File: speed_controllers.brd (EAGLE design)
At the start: 147.3 x 147.3 mm, 46 parts, among them M1 TE-1-1123723-3, M2 TE-1-1123723-3, M3 TE-1-1123723-3, M4 TE-1-1123723-3, M5 TE-1-1123723-3, M6 TE-1-1123723-3, M7 TE-1-1123723-3, M8 TE-1-1123723-3

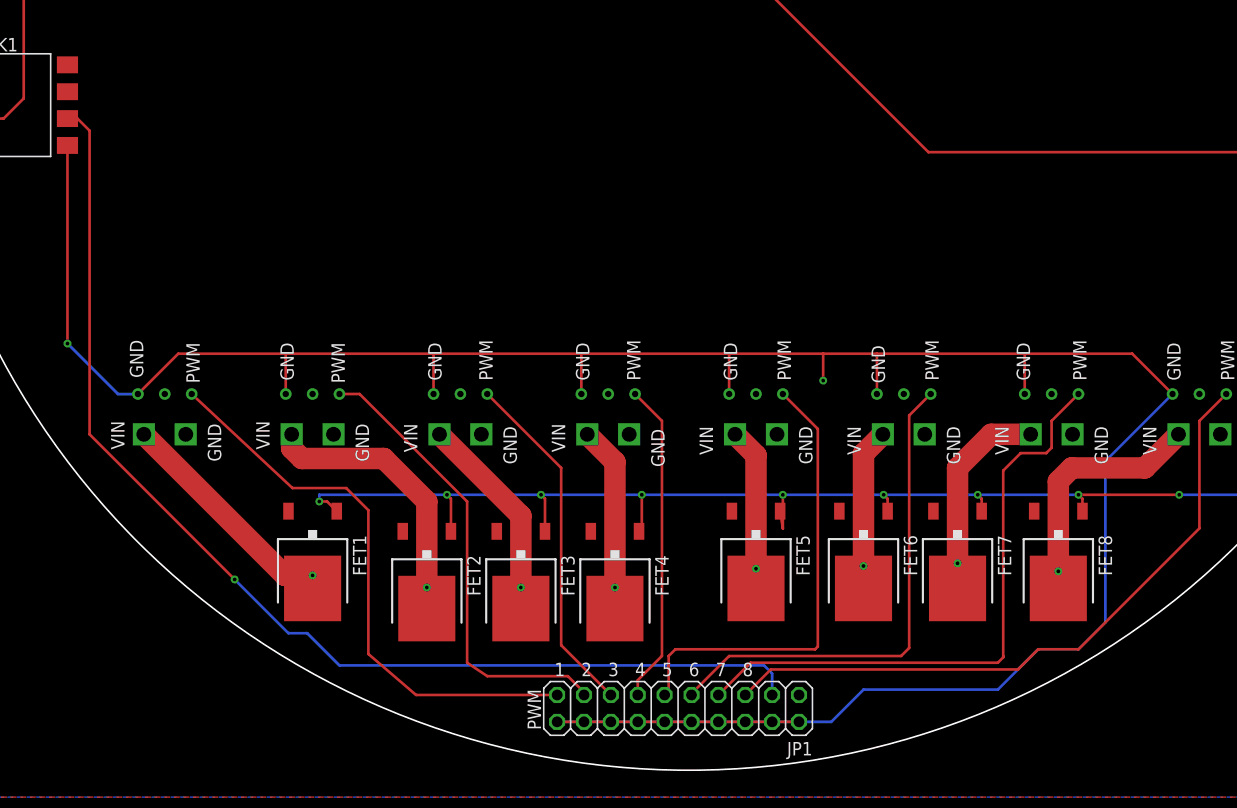
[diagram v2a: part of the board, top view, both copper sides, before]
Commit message: Changed Optocoupler circuit
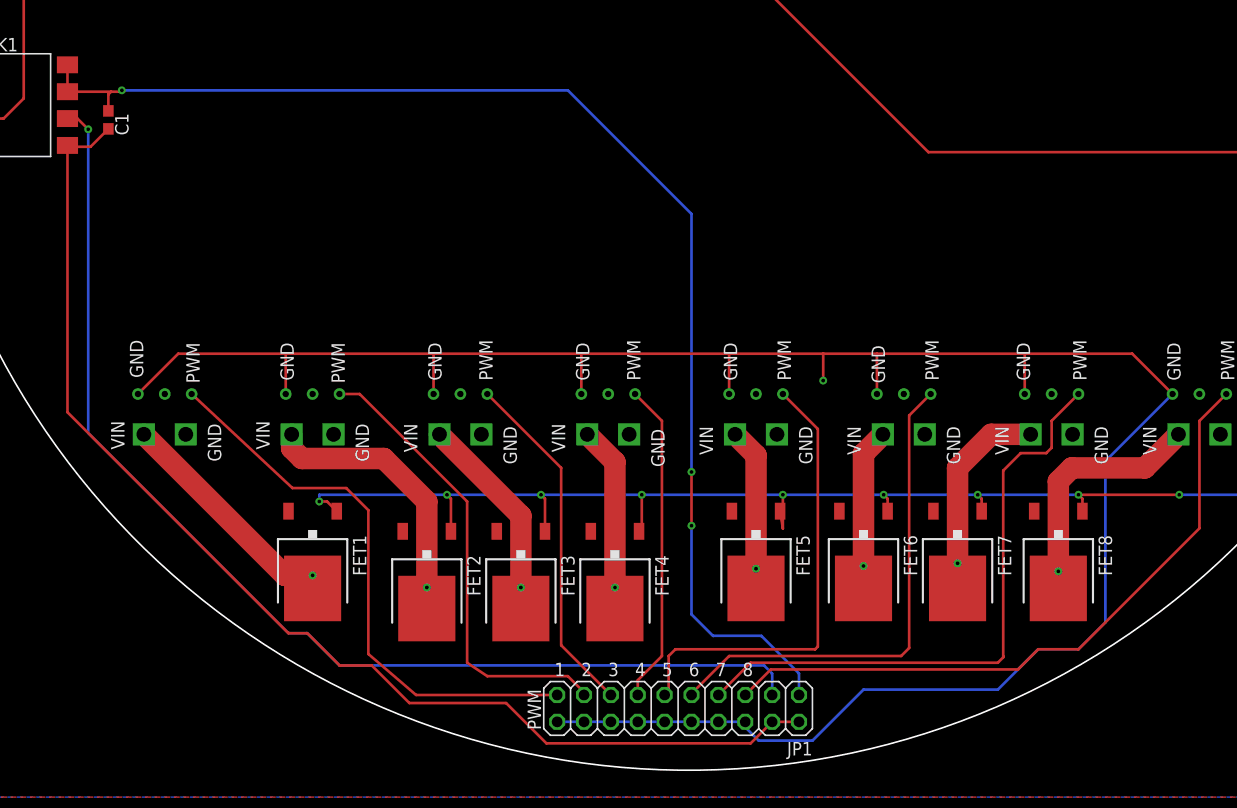
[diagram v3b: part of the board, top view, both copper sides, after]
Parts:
- added C1: 100nF, rcl:C0603
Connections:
- new net MCU_GND: C1.2, JP1.2, JP1.4, OK1.5
- new net MCU_VCC: C1.1, JP1.1, OK1.7, OK1.8
- net PWM_GND: no longer JP1.2, JP1.4, OK1.5
- net VCC: no longer OK1.7, OK1.8
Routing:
- net MCU_VCC: track 0.00 -> 120.7 mm, vias 0 -> 3
- net MCU_GND: track 0.00 -> 112.7 mm
- net PWM_GND: track 256.5 -> 208.0 mm, vias 2 -> 1

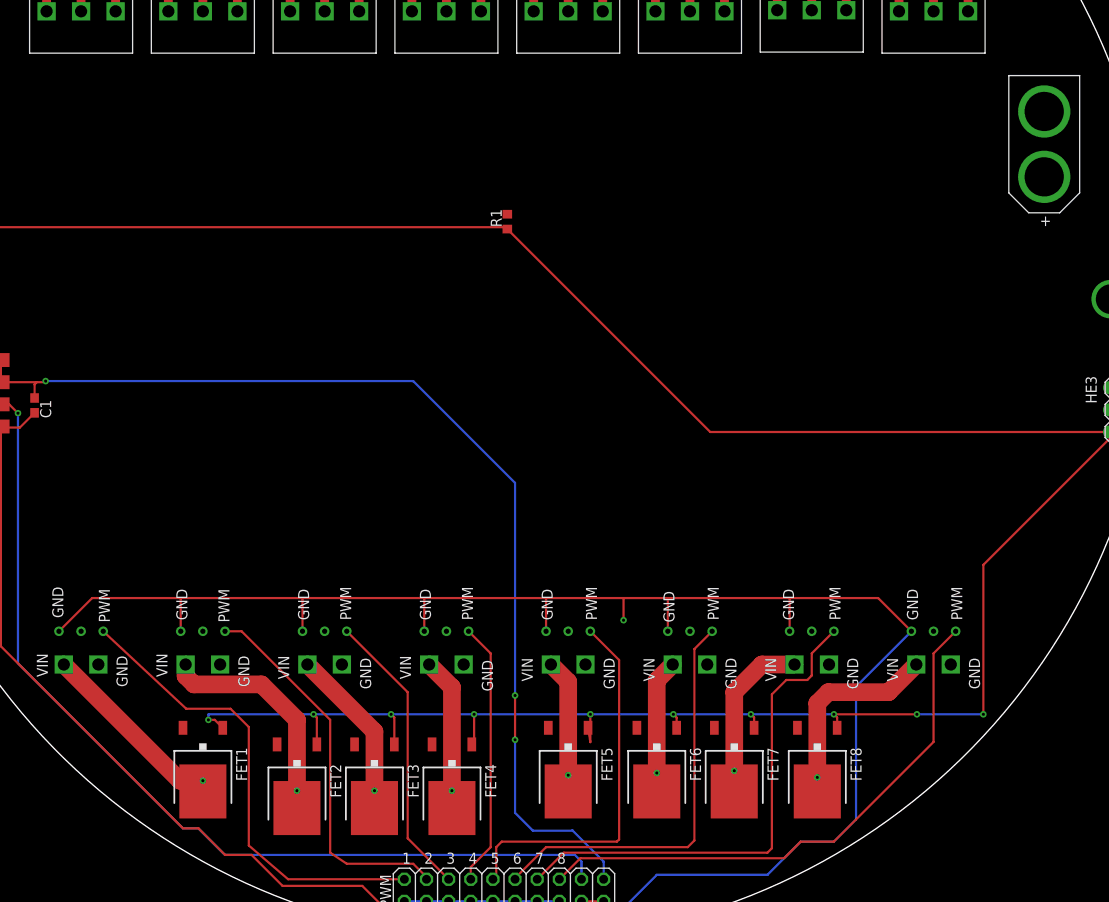
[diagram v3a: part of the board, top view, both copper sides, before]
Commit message: Redid PWM and moved silkscreen for the XT-60
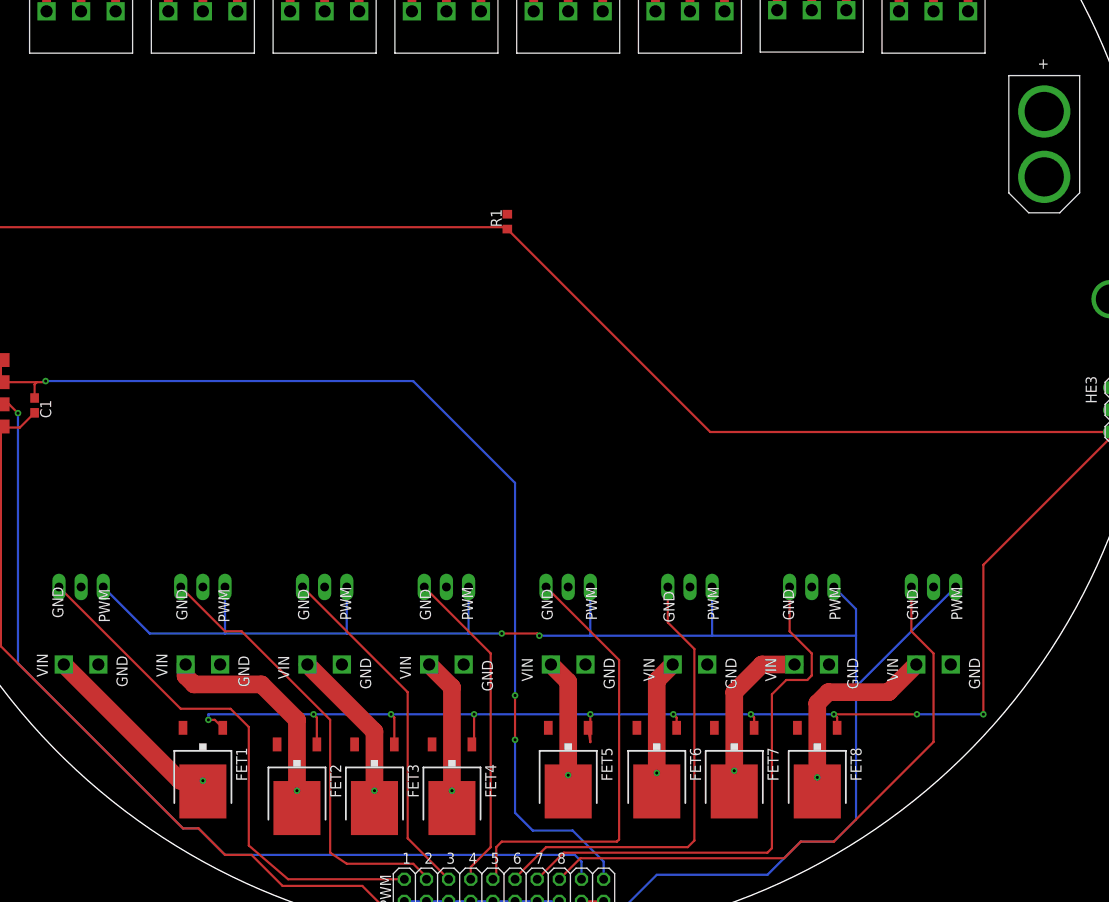
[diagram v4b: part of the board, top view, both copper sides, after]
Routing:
- net PWM_GND: track 208.0 -> 217.2 mm, vias 1 -> 2
- net SIG_1: track 53.9 -> 61.3 mm
- net SIG_4: track 30.8 -> 38.0 mm
- net SIG_5: track 43.5 -> 50.7 mm
- net SIG_3: track 33.3 -> 40.5 mm
- net SIG_2: track 43.8 -> 51.0 mm
- net SIG_6: track 47.3 -> 52.8 mm
- net SIG_8: track 63.2 -> 68.3 mm
- net SIG_7: track 57.6 -> 62.7 mm
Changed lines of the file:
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@@
 <text x="-44.196" y="-40.894" size="1.27" layer="26" rot="MR270">GND</text>
 <text x="-53.34" y="-40.64" size="1.27" layer="26" rot="MR270">VIN</text>
-<text x="60.452" y="8.382" size="1.27" layer="25">+</text>
+<text x="60.198" y="26.416" size="1.27" layer="25">+</text>
 </plain>
 <attributes>
@@
 <contactref element="MOTOR6" pad="PWM_GND"/>
 <contactref element="MOTOR5" pad="PWM_GND"/>
-<wire x1="45.72" y1="-38.1" x2="39.37" y2="-44.45" width="0.254" layer="16"/>
+<wire x1="50.8" y1="-33.02" x2="39.37" y2="-44.45" width="0.254" layer="16"/>
 <wire x1="39.37" y1="-44.45" x2="39.37" y2="-59.69" width="0.254" layer="16"/>
 <wire x1="39.37" y1="-59.69" x2="36.83" y2="-62.23" width="0.254" layer="16"/>
@@
 <contactref element="MOTOR3" pad="PWM_GND"/>
 <contactref element="MOTOR4" pad="PWM_GND"/>
-<wire x1="-52.07" y1="-38.1" x2="-48.26" y2="-34.29" width="0.254" layer="1"/>
-<wire x1="-48.26" y1="-34.29" x2="-38.1" y2="-34.29" width="0.254" layer="1"/>
-<wire x1="-38.1" y1="-34.29" x2="-24.13" y2="-34.29" width="0.254" layer="1"/>
-<wire x1="-24.13" y1="-34.29" x2="-10.16" y2="-34.29" width="0.254" layer="1"/>
-<wire x1="-10.16" y1="-34.29" x2="3.81" y2="-34.29" width="0.254" layer="1"/>
-<wire x1="3.81" y1="-34.29" x2="12.7" y2="-34.29" width="0.254" layer="1"/>
-<wire x1="12.7" y1="-34.29" x2="17.78" y2="-34.29" width="0.254" layer="1"/>
-<wire x1="17.78" y1="-34.29" x2="31.75" y2="-34.29" width="0.254" layer="1"/>
-<wire x1="41.91" y1="-34.29" x2="31.75" y2="-34.29" width="0.254" layer="1"/>
-<wire x1="-10.16" y1="-38.1" x2="-10.16" y2="-34.29" width="0.254" layer="1"/>
-<wire x1="-24.13" y1="-38.1" x2="-24.13" y2="-34.29" width="0.254" layer="1"/>
-<wire x1="-38.1" y1="-38.1" x2="-38.1" y2="-34.29" width="0.254" layer="1"/>
-<wire x1="12.7" y1="-34.29" x2="12.7" y2="-36.83" width="0.254" layer="1"/>
-<via x="12.7" y="-36.83" extent="1-16" drill="0.35"/>
 <contactref element="JP1" pad="20"/>
 <contactref element="JP1" pad="18"/>
@@
 <wire x1="5.334" y1="-69.596" x2="5.334" y2="-69.088" width="0.254" layer="16"/>
 <wire x1="16.51" y1="-66.04" x2="11.684" y2="-70.866" width="0.254" layer="16"/>
-<wire x1="3.81" y1="-38.1" x2="3.81" y2="-34.29" width="0.254" layer="1"/>
-<wire x1="17.78" y1="-38.1" x2="17.78" y2="-34.29" width="0.254" layer="1"/>
-<wire x1="31.75" y1="-38.1" x2="31.75" y2="-34.29" width="0.254" layer="1"/>
-<wire x1="45.72" y1="-38.1" x2="41.91" y2="-34.29" width="0.254" layer="1"/>
+<wire x1="39.37" y1="-44.45" x2="39.37" y2="-38.608" width="0.254" layer="16"/>
+<wire x1="39.37" y1="-38.608" x2="39.37" y2="-35.56" width="0.254" layer="16"/>
+<wire x1="39.37" y1="-35.56" x2="36.83" y2="-33.02" width="0.254" layer="16"/>
+<wire x1="39.37" y1="-38.608" x2="22.86" y2="-38.608" width="0.254" layer="16"/>
+<via x="3.048" y="-38.608" extent="1-16" drill="0.35"/>
+<wire x1="22.86" y1="-38.608" x2="8.89" y2="-38.608" width="0.254" layer="16"/>
+<wire x1="8.89" y1="-38.608" x2="3.048" y2="-38.608" width="0.254" layer="16"/>
+<wire x1="3.048" y1="-38.608" x2="2.794" y2="-38.354" width="0.254" layer="1"/>
+<wire x1="2.794" y1="-38.354" x2="-1.27" y2="-38.354" width="0.254" layer="1"/>
+<via x="-1.27" y="-38.354" extent="1-16" drill="0.35"/>
+<wire x1="-1.27" y1="-38.354" x2="-5.08" y2="-38.354" width="0.254" layer="16"/>
+<wire x1="-5.08" y1="-38.354" x2="-19.05" y2="-38.354" width="0.254" layer="16"/>
+<wire x1="-19.05" y1="-38.354" x2="-33.02" y2="-38.354" width="0.254" layer="16"/>
+<wire x1="-33.02" y1="-38.354" x2="-41.656" y2="-38.354" width="0.254" layer="16"/>
+<wire x1="-41.656" y1="-38.354" x2="-46.99" y2="-33.02" width="0.254" layer="16"/>
+<wire x1="-33.02" y1="-33.02" x2="-33.02" y2="-38.354" width="0.254" layer="16"/>
+<wire x1="-19.05" y1="-33.02" x2="-19.05" y2="-38.354" width="0.254" layer="16"/>
+<wire x1="-5.08" y1="-33.02" x2="-5.08" y2="-38.354" width="0.254" layer="16"/>
+<wire x1="8.89" y1="-33.02" x2="8.89" y2="-38.608" width="0.254" layer="16"/>
+<wire x1="22.86" y1="-33.02" x2="22.86" y2="-38.608" width="0.254" layer="16"/>
 </signal>
 <signal name="VIN_7">
@@
 <signal name="SIG_7">
 <contactref element="MOTOR7" pad="PWM_SIG"/>
-<wire x1="34.29" y1="-40.64" x2="36.83" y2="-38.1" width="0.254" layer="1"/>
-<wire x1="29.718" y1="-45.339" x2="29.718" y2="-62.865" width="0.254" layer="1"/>
+<wire x1="29.718" y1="-45.339" x2="29.718" y2="-62.992" width="0.254" layer="1"/>
 <wire x1="34.29" y1="-43.18" x2="34.29" y2="-40.64" width="0.254" layer="1"/>
 <wire x1="29.718" y1="-45.339" x2="31.369" y2="-43.688" width="0.254" layer="1"/>
@@
 <wire x1="5.842" y1="-63.5" x2="29.21" y2="-63.5" width="0.254" layer="1"/>
 <wire x1="29.21" y1="-63.5" x2="29.718" y2="-62.992" width="0.254" layer="1"/>
-<wire x1="29.718" y1="-62.992" x2="29.718" y2="-62.865" width="0.254" layer="1"/>
+<wire x1="34.29" y1="-40.64" x2="31.75" y2="-38.1" width="0.254" layer="1"/>
+<wire x1="31.75" y1="-38.1" x2="31.75" y2="-33.02" width="0.254" layer="1"/>
 </signal>
 <signal name="SIG_8">
 <contactref element="MOTOR8" pad="PWM_SIG"/>
 <wire x1="48.26" y1="-50.8" x2="48.26" y2="-40.64" width="0.254" layer="1"/>
-<wire x1="48.26" y1="-40.64" x2="50.8" y2="-38.1" width="0.254" layer="1"/>
 <wire x1="33.02" y1="-62.23" x2="36.83" y2="-62.23" width="0.254" layer="1"/>
 <wire x1="36.83" y1="-62.23" x2="48.26" y2="-50.8" width="0.254" layer="1"/>
@@
 <wire x1="7.747" y1="-64.135" x2="31.115" y2="-64.135" width="0.254" layer="1"/>
 <wire x1="31.115" y1="-64.135" x2="33.02" y2="-62.23" width="0.254" layer="1"/>
+<wire x1="48.26" y1="-40.64" x2="45.72" y2="-38.1" width="0.254" layer="1"/>
+<wire x1="45.72" y1="-38.1" x2="45.72" y2="-33.02" width="0.254" layer="1"/>
 </signal>
 <signal name="VIN_1">
@@
 <contactref element="MOTOR6" pad="PWM_SIG"/>
 <wire x1="20.828" y1="-40.132" x2="20.828" y2="-62.103" width="0.254" layer="1"/>
-<wire x1="20.828" y1="-40.132" x2="22.86" y2="-38.1" width="0.254" layer="1"/>
 <contactref element="JP1" pad="9"/>
 <wire x1="20.828" y1="-62.103" x2="20.066" y2="-62.865" width="0.254" layer="1"/>
@@
 <wire x1="3.81" y1="-62.865" x2="0.254" y2="-66.421" width="0.254" layer="1"/>
 <wire x1="0.254" y1="-66.421" x2="0.254" y2="-66.548" width="0.254" layer="1"/>
+<wire x1="17.78" y1="-33.02" x2="17.78" y2="-37.084" width="0.254" layer="1"/>
+<wire x1="17.78" y1="-37.084" x2="20.828" y2="-40.132" width="0.254" layer="1"/>
 </signal>
 <signal name="SIG_5">
 <contactref element="MOTOR5" pad="PWM_SIG"/>
-<wire x1="8.89" y1="-38.1" x2="12.192" y2="-41.402" width="0.254" layer="1"/>
+<wire x1="3.81" y1="-33.02" x2="12.192" y2="-41.402" width="0.254" layer="1"/>
 <wire x1="12.192" y1="-41.402" x2="12.192" y2="-61.976" width="0.254" layer="1"/>
 <wire x1="11.938" y1="-62.23" x2="12.192" y2="-61.976" width="0.254" layer="1"/>
@@
 <signal name="SIG_4">
 <contactref element="MOTOR4" pad="PWM_SIG"/>
-<wire x1="-5.08" y1="-38.1" x2="-2.54" y2="-40.64" width="0.254" layer="1"/>
+<wire x1="-10.16" y1="-33.02" x2="-2.54" y2="-40.64" width="0.254" layer="1"/>
 <contactref element="JP1" pad="13"/>
 <wire x1="-5.08" y1="-66.294" x2="-4.826" y2="-66.548" width="0.254" layer="1"/>
@@
 <signal name="SIG_3">
 <contactref element="MOTOR3" pad="PWM_SIG"/>
-<wire x1="-19.05" y1="-38.1" x2="-12.065" y2="-45.085" width="0.254" layer="1"/>
+<wire x1="-24.13" y1="-33.02" x2="-12.065" y2="-45.085" width="0.254" layer="1"/>
 <wire x1="-12.065" y1="-45.085" x2="-12.065" y2="-61.849" width="0.254" layer="1"/>
 <contactref element="JP1" pad="15"/>
@@
 <contactref element="JP1" pad="17"/>
 <wire x1="-9.906" y1="-66.294" x2="-9.906" y2="-66.548" width="0.254" layer="1"/>
-<wire x1="-31.115" y1="-38.1" x2="-33.02" y2="-38.1" width="0.254" layer="1"/>
 <wire x1="-20.955" y1="-48.26" x2="-20.955" y2="-63.5" width="0.254" layer="1"/>
 <wire x1="-20.955" y1="-48.26" x2="-31.115" y2="-38.1" width="0.254" layer="1"/>
@@
 <wire x1="-19.05" y1="-64.77" x2="-11.43" y2="-64.77" width="0.254" layer="1"/>
 <wire x1="-11.43" y1="-64.77" x2="-9.906" y2="-66.294" width="0.254" layer="1"/>
+<wire x1="-31.115" y1="-38.1" x2="-33.02" y2="-38.1" width="0.254" layer="1"/>
+<wire x1="-33.02" y1="-38.1" x2="-38.1" y2="-33.02" width="0.254" layer="1"/>
 </signal>
 <signal name="SIG_1">
@@
 <wire x1="-25.781" y1="-66.548" x2="-30.2895" y2="-62.6745" width="0.254" layer="1"/>
 <wire x1="-30.2895" y1="-62.6745" x2="-30.2895" y2="-49.0855" width="0.254" layer="1"/>
-<wire x1="-37.465" y1="-46.99" x2="-46.99" y2="-38.1" width="0.254" layer="1"/>
 <contactref element="JP1" pad="19"/>
 <wire x1="-25.781" y1="-66.548" x2="-12.446" y2="-66.548" width="0.254" layer="1"/>
-<wire x1="-30.2895" y1="-49.0855" x2="-32.385" y2="-46.99" width="0.254" layer="1"/>
-<wire x1="-32.385" y1="-46.99" x2="-37.465" y2="-46.99" width="0.254" layer="1"/>
+<wire x1="-32.385" y1="-46.99" x2="-30.2895" y2="-49.0855" width="0.254" layer="1"/>
+<wire x1="-52.07" y1="-33.02" x2="-38.1" y2="-46.99" width="0.254" layer="1"/>
+<wire x1="-38.1" y1="-46.99" x2="-32.385" y2="-46.99" width="0.254" layer="1"/>
 </signal>
 <signal name="VIN_4">

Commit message: Changed board to not have anything within a 5 inch diameter on the back side
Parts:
- added R10: 10k, auv:R0603
- moved JP1 123.2 mm to (0.25, 55.4)
- moved R1 70.2 mm to (-64.8, -19.7), turned to 180 degrees
- moved U$1 54.5 mm to (6.60, 14.2)
- moved HE2 35.5 mm to (-54.5, -21.5), turned to 90 degrees
- moved HE3 17.6 mm to (54.0, -21.6)
- moved MOTOR2 16.9 mm to (-31.8, 17.8), flipped to the top
- moved MOTOR4 16.6 mm to (-6.35, 17.8), flipped to the top
- moved MOTOR6 16.6 mm to (19.1, 17.8), flipped to the top
- moved M1 14.8 mm to (-44.6, 19.1), flipped to the bottom
- moved M2 14.5 mm to (-31.8, 19.1), flipped to the bottom
- moved M8 14.5 mm to (44.5, 19.1), flipped to the bottom
- moved M4 14.0 mm to (-6.35, 19.1), flipped to the bottom
- moved M6 14.0 mm to (19.1, 19.1), flipped to the bottom
- moved M7 10.5 mm to (31.8, 43.3), flipped to the bottom
- moved M3 10.5 mm to (-19.1, 43.2), flipped to the bottom
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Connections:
- new net N$4: OK1.2, R10.1
- net VCC: now also R10.2; no longer OK1.2
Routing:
- net FET_G: track 323.8 -> 188.0 mm, vias 10 -> 9
- net SIG_5: track 50.7 -> 180.3 mm
- net SIG_4: track 38.0 -> 162.8 mm
- net SIG_3: track 40.5 -> 162.4 mm, vias 0 -> 1
- net KILL_SWITCH_OPTO: track 107.4 -> 222.3 mm, vias 1 -> 4
- net SIG_6: track 52.8 -> 158.7 mm
- net SIG_7: track 62.7 -> 146.6 mm, vias 0 -> 1
- net SIG_2: track 51.0 -> 130.2 mm
- net PWM_GND: track 217.2 -> 288.3 mm, vias 2 -> 1
- net SIG_1: track 61.3 -> 131.9 mm, vias 0 -> 1
- net MCU_VCC: track 120.7 -> 189.3 mm, vias 3 -> 2
- net SIG_8: track 68.3 -> 134.3 mm
- net MCU_GND: track 112.7 -> 162.9 mm, vias 0 -> 3
- net M6_3: track 11.6 -> 24.3 mm
- net M6_2: track 11.6 -> 24.3 mm
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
